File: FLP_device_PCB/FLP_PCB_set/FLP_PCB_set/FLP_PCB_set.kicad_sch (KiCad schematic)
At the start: 0 parts

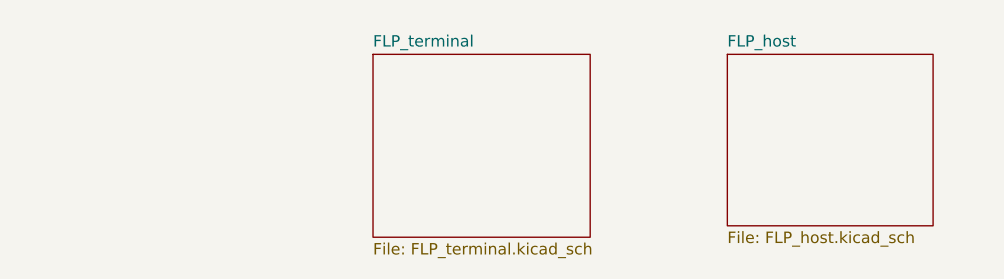
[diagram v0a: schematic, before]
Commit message: PCB fixing end adding description pdf
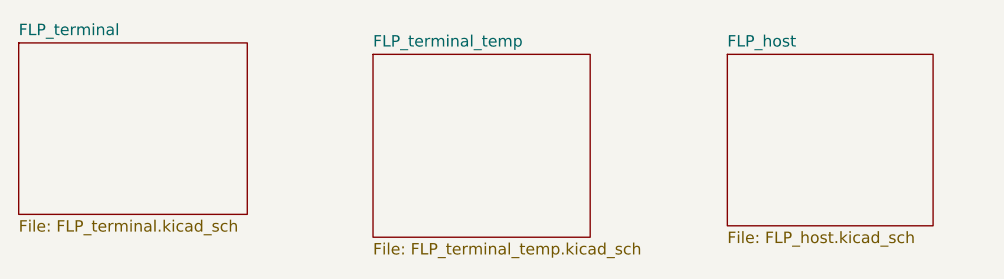
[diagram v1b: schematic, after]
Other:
- added sheet FLP_terminal_temp (FLP_terminal_temp.kicad_sch)
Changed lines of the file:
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@@
+	)
+	(sheet
+		(at 85.09 132.08)
+		(size 25.4 19.05)
+		(exclude_from_sim no)
+		(in_bom yes)
+		(on_board yes)
+		(dnp no)
+		(fields_autoplaced yes)
+		(stroke
+			(width 0.1524)
+			(type solid)
+		)
+		(fill
+			(color 0 0 0 0.0000)
+		)
+		(property "Sheetname" "FLP_terminal"
+			(at 85.09 131.3684 0)
+			(effects
+				(font
+					(size 1.27 1.27)
+				)
+				(justify left bottom)
+			)
+		)
+		(property "Sheetfile" "FLP_terminal.kicad_sch"
+			(at 85.09 151.7146 0)
+			(effects
+				(font
+					(size 1.27 1.27)
+				)
+				(justify left top)
+			)
+		)
+		(instances
+			(project "FLP_PCB_set"
+				(path "/3f8c5218-62bd-4afc-a38b-629e4a961e52"
+					(page "13")
+				)
+			)
+		)
 	)
 	(sheet
@@
 			(color 0 0 0 0.0000)
 		)
-		(property "Sheetname" "FLP_terminal"
+		(property "Sheetname" "FLP_terminal_temp"
 			(at 124.46 132.6384 0)
 			(effects
@@
 			)
 		)
-		(property "Sheetfile" "FLP_terminal.kicad_sch"
+		(property "Sheetfile" "FLP_terminal_temp.kicad_sch"
 			(at 124.46 154.2546 0)
 			(effects

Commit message: PCB pdf add
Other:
- removed sheet FLP_terminal
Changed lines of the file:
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@@
-	)
-	(sheet
-		(at 85.09 132.08)
-		(size 25.4 19.05)
-		(exclude_from_sim no)
-		(in_bom yes)
-		(on_board yes)
-		(dnp no)
-		(fields_autoplaced yes)
-		(stroke
-			(width 0.1524)
-			(type solid)
-		)
-		(fill
-			(color 0 0 0 0.0000)
-		)
-		(property "Sheetname" "FLP_terminal"
-			(at 85.09 131.3684 0)
-			(effects
-				(font
-					(size 1.27 1.27)
-				)
-				(justify left bottom)
-			)
-		)
-		(property "Sheetfile" "FLP_terminal.kicad_sch"
-			(at 85.09 151.7146 0)
-			(effects
-				(font
-					(size 1.27 1.27)
-				)
-				(justify left top)
-			)
-		)
-		(instances
-			(project "FLP_PCB_set"
-				(path "/3f8c5218-62bd-4afc-a38b-629e4a961e52"
-					(page "13")
-				)
-			)
-		)
 	)
 	(sheet
